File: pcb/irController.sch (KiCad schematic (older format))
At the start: 35 parts, among them IC1 ADT7410TRZ, J1 B4B-PH-K-S(LF)(SN), P1 ZX62R-B-5P, Q1 Q_NMOS, SW1 SKRPACE010, SW2 SKRPACE010, U1 NJM2845, U2 ESP-13-WROOM-02, U3 IRSNS_GP1UXC41QS

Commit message: LEDの駆動電流は5V固定にした
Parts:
- removed JP1: SolderJumper_3_Open, Jumper:SolderJumper-3_P1.3mm_Open_RoundedPad1.0x1.5mm_NumberLabels, symbol Jumper:SolderJumper_3_Open
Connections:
- net +5V: now also D1.2 (A), D2.2 (A), D3.2 (A)
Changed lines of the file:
@@
 Connection ~ 8000 2300
-$Comp
-L Jumper:SolderJumper_3_Open JP1
-U 1 1 5E8354F2
-P 9400 1800
-F 0 "JP1" H 9400 2005 50  0000 C CNN
-F 1 "SolderJumper_3_Open" H 9400 1914 50  0000 C CNN
-F 2 "Jumper:SolderJumper-3_P1.3mm_Open_RoundedPad1.0x1.5mm_NumberLabels" H 9400 1800 50  0001 C CNN
-F 3 "~" H 9400 1800 50  0001 C CNN
-	1    9400 1800
-	1    0    0    -1
-$EndComp
 $Comp
 L power:+5V #PWR0107
@@
 	9400 1950 9400 2300
 Connection ~ 9400 2300
-Wire Wire Line
-	9200 1800 8800 1800
-Wire Wire Line
-	8800 1800 8800 1450
-$Comp
-L power:+3V3 #PWR0108
-U 1 1 5E84B46E
-P 8800 1450
-F 0 "#PWR0108" H 8800 1300 50  0001 C CNN
-F 1 "+3V3" H 8815 1623 50  0000 C CNN
-F 2 "" H 8800 1450 50  0001 C CNN
-F 3 "" H 8800 1450 50  0001 C CNN
-	1    8800 1450
-	1    0    0    -1
-$EndComp
 $Comp
 L power:+5V #PWR0109
 U 1 1 5E84B8AF
-P 10050 1400
-F 0 "#PWR0109" H 10050 1250 50  0001 C CNN
-F 1 "+5V" H 10065 1573 50  0000 C CNN
-F 2 "" H 10050 1400 50  0001 C CNN
-F 3 "" H 10050 1400 50  0001 C CNN
-	1    10050 1400
+P 9400 1950
+F 0 "#PWR0109" H 9400 1800 50  0001 C CNN
+F 1 "+5V" H 9415 2123 50  0000 C CNN
+F 2 "" H 9400 1950 50  0001 C CNN
+F 3 "" H 9400 1950 50  0001 C CNN
+	1    9400 1950
 	1    0    0    -1
 $EndComp
-Wire Wire Line
-	9600 1800 10050 1800
-Wire Wire Line
-	10050 1800 10050 1400
 $EndSCHEMATC

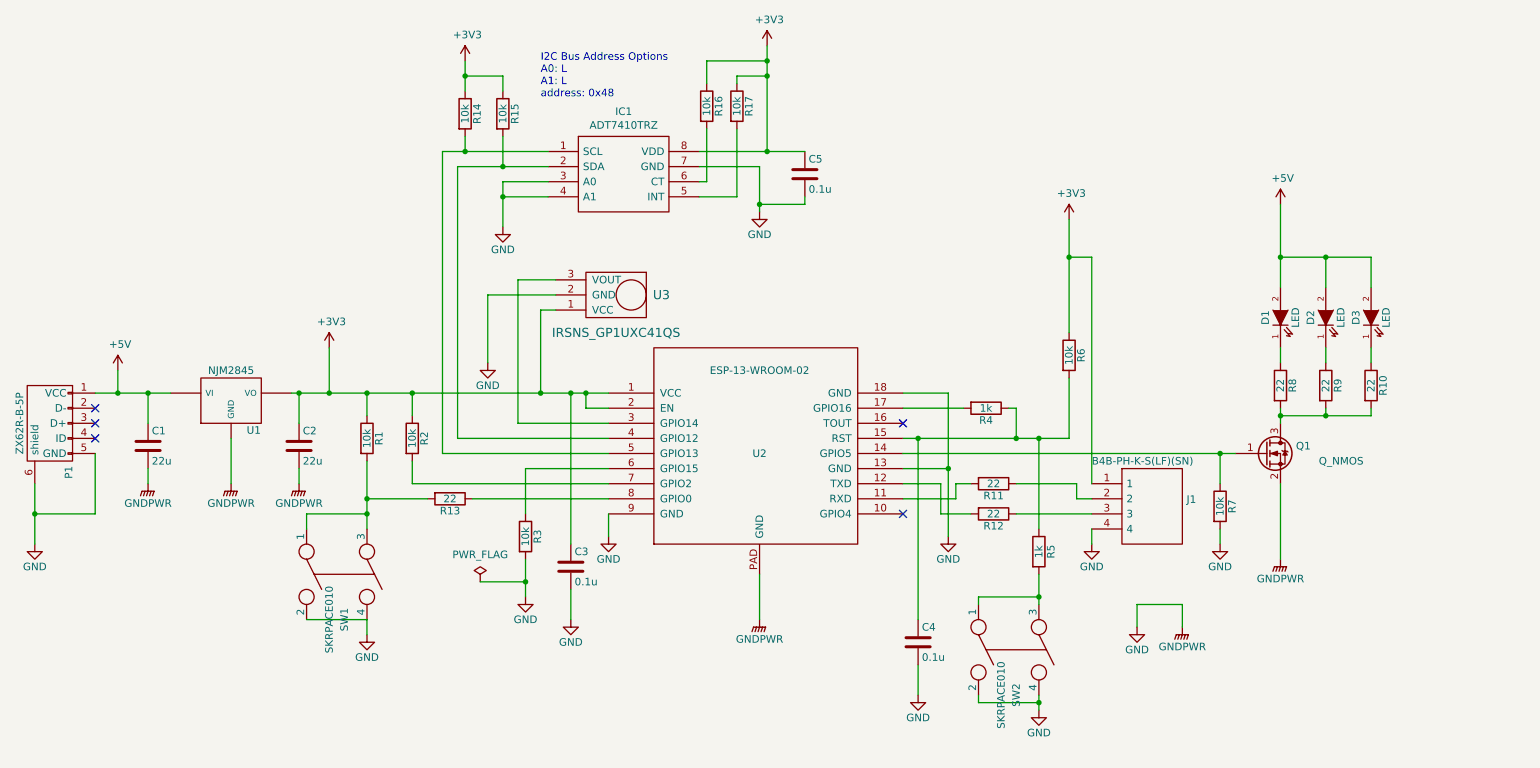
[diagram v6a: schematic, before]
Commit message: IC発熱を考慮して再配置
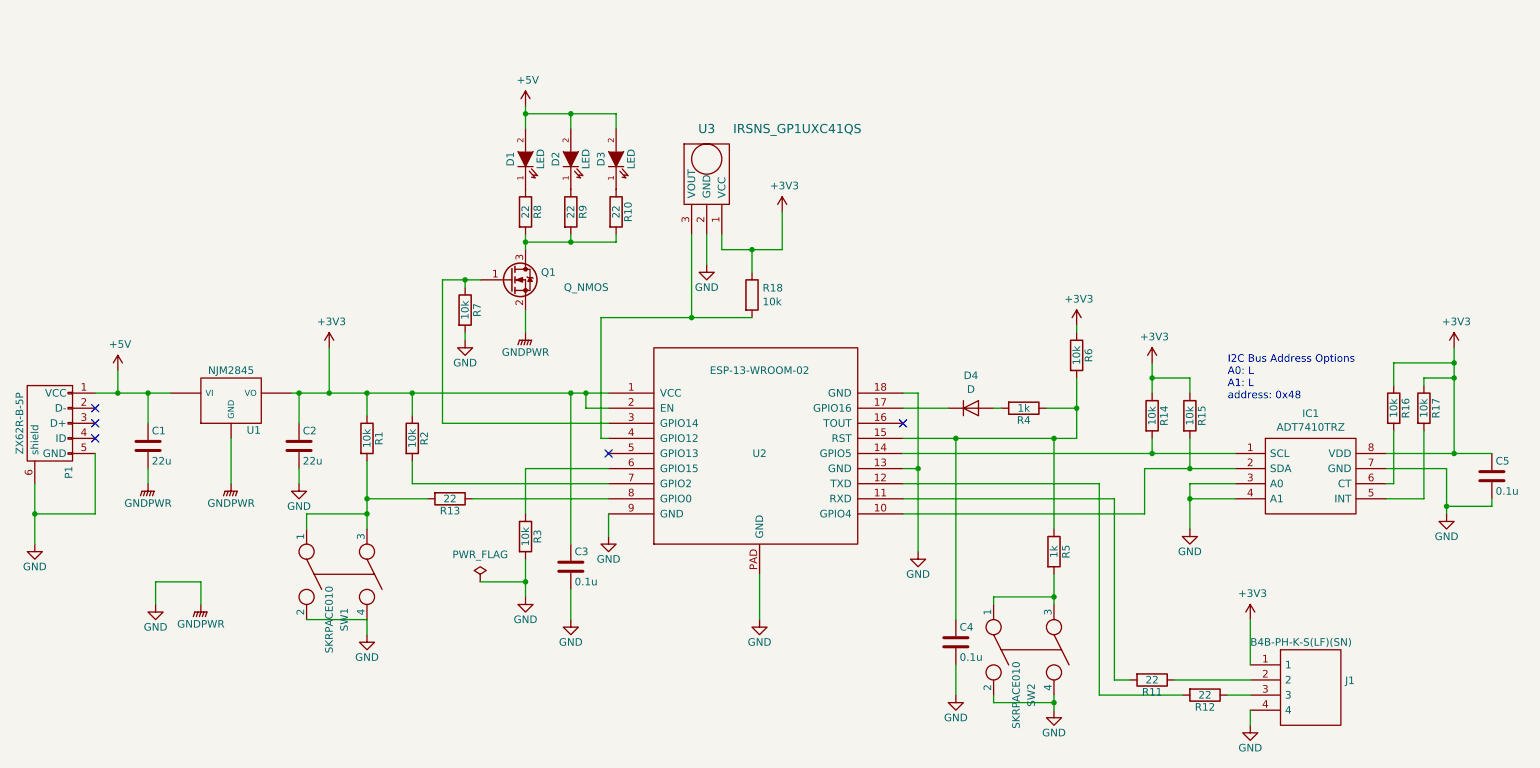
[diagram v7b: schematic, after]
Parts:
- added D4: D, Diode_SMD:D_SOD-123F, symbol Device:D
- added R18: 10k, Resistor_SMD:R_0603_1608Metric, symbol Device:R
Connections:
- net +3V3: now also R18.1
- net at U2.10 (GPIO4): now also IC1.2 (SDA), R15.2
- net at Q1.1 (G), R7.1: now also U2.3 (GPIO14); no longer U2.14 (GPIO5)
- net at U2.17 (GPIO16): now also D4.1 (K); no longer R4.2
- net at U3.3 (VOUT): now also U2.4 (GPIO12), R18.2; no longer U2.3 (GPIO14)
- net at IC1.1 (SCL), R14.2: now also U2.14 (GPIO5); no longer U2.5 (GPIO13)
- new net: D4.2 (A), R4.2
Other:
- moved on the sheet: C4, C5, D1, D2, D3, IC1, J1, Q1, R10, R11, R12, R14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

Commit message: tmp
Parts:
- added R19: 10k, Resistor_SMD:R_0603_1608Metric, symbol Device:R
- added U4: DHT11, Connector_PinHeader_2.54mm:PinHeader_1x04_P2.54mm_Vertical, symbol Sensor:DHT11
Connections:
- net +3V3: now also R19.1, U4.1 (VCC)
- net GND: now also U4.4 (GND)
- net at U2.5 (GPIO13): now also R19.2, U4.2 (IO)
- no-connect marks 5 -> 4
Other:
- note added: "GP1UXC41QS is not require \na pull-up resistor.\nFor alternative IC."
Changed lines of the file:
@@
 P 5600 1750
 F 0 "U3" H 5600 2050 60  0000 C CNN
-F 1 "IRSNS_GP1UXC41QS" H 6200 2050 60  0000 C CNN
+F 1 "IRSNS_GP1UXC41QS" H 5600 2150 60  0000 C CNN
 F 2 "Socket_Strips:Socket_Strip_Straight_1x03" H 5700 1550 60  0001 C CNN
 F 3 "" H 5700 1550 60  0000 C CNN
@@
 $EndComp
 Wire Wire Line
-	4950 3500 4900 3500
-Wire Wire Line
-	4900 3500 4900 2700
+	4950 3500 4650 3500
+Wire Wire Line
+	4650 3500 4650 2700
 Wire Wire Line
 	5700 2250 5900 2250
@@
 	5500 2150 5500 2700
 Wire Wire Line
-	4900 2700 5500 2700
-NoConn ~ 4950 3600
+	4650 2700 5500 2700
 $Comp
 L Device:R R18
@@
 Wire Wire Line
 	6900 3900 8300 3900
+$Comp
+L Sensor:DHT11 U4
+U 1 1 5EA7525E
+P 6850 1800
+F 0 "U4" H 6606 1846 50  0000 R CNN
+F 1 "DHT11" H 6606 1755 50  0000 R CNN
+F 2 "Connector_PinHeader_2.54mm:PinHeader_1x04_P2.54mm_Vertical" H 6850 1400 50  0001 C CNN
+F 3 "http://akizukidenshi.com/download/ds/aosong/DHT11.pdf" H 7000 2050 50  0001 C CNN
+	1    6850 1800
+	1    0    0    -1
+$EndComp
+$Comp
+L irController-rescue:GND #PWR022
+U 1 1 5EA765C4
+P 6850 2250
+F 0 "#PWR022" H 6850 2000 50  0001 C CNN
+F 1 "GND" H 6850 2100 50  0000 C CNN
+F 2 "" H 6850 2250 50  0000 C CNN
+F 3 "" H 6850 2250 50  0000 C CNN
+	1    6850 2250
+	1    0    0    -1
+$EndComp
+Wire Wire Line
+	6850 2250 6850 2100
+$Comp
+L power:+3V3 #PWR021
+U 1 1 5EA7C4EC
+P 6850 1300
+F 0 "#PWR021" H 6850 1150 50  0001 C CNN
+F 1 "+3V3" H 6865 1473 50  0000 C CNN
+F 2 "" H 6850 1300 50  0001 C CNN
+F 3 "" H 6850 1300 50  0001 C CNN
+	1    6850 1300
+	1    0    0    -1
+$EndComp
+Wire Wire Line
+	6850 1300 6850 1400
+$Comp
+L Device:R R19
+U 1 1 5EA82532
+P 7300 1600
+F 0 "R19" H 7370 1646 50  0000 L CNN
+F 1 "10k" H 7370 1555 50  0000 L CNN
+F 2 "Resistor_SMD:R_0603_1608Metric" V 7230 1600 50  0001 C CNN
+F 3 "~" H 7300 1600 50  0001 C CNN
+	1    7300 1600
+	1    0    0    -1
+$EndComp
+Wire Wire Line
+	6850 1400 7300 1400
+Connection ~ 6850 1400
+Wire Wire Line
+	6850 1400 6850 1500
+Wire Wire Line
+	7150 1800 7250 1800
+Wire Wire Line
+	7250 1800 7250 2800
+Wire Wire Line
+	7250 2800 4850 2800
+Wire Wire Line
+	4850 2800 4850 3600
+Wire Wire Line
+	4850 3600 4950 3600
+Connection ~ 7250 1800
+Wire Wire Line
+	7250 1800 7300 1800
+Wire Wire Line
+	7300 1800 7300 1750
+Wire Wire Line
+	7300 1450 7300 1400
+Text Notes 5250 1200 0    50   ~ 0
+GP1UXC41QS is not require \na pull-up resistor.\nFor alternative IC.
 $EndSCHEMATC
